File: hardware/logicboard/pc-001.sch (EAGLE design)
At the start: 15 parts, among them J4 DNP, J5 DNP

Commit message: OSHW logo.
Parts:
- added LOGO1: OSHW-LOGOL, SparkFun-Aesthetics:OSHW-LOGOL
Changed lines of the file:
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@@
 <part name="MMA8452Q" library="SparkFun-Connectors" library_urn="urn:adsk.eagle:library:513" deviceset="CONN_06" device="NO_SILK_FEMALE_PTH" package3d_urn="urn:adsk.eagle:package:38130/1"/>
 <part name="FRAME2" library="frames" library_urn="urn:adsk.eagle:library:229" deviceset="A4L-LOC" device=""/>
+<part name="LOGO1" library="SparkFun-Aesthetics" deviceset="OSHW-LOGO" device="L"/>
 </parts>
 <sheets>
@@
 <instance part="MMA8452Q" gate="G$1" x="187.96" y="86.36" rot="R180"/>
 <instance part="FRAME2" gate="G$1" x="0" y="0"/>
+<instance part="LOGO1" gate="G$1" x="200.66" y="15.24"/>
 </instances>
 <busses>

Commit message: Pineapple logo v2.
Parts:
- added U$1: PINEAPPLELOGO2, pineapplelogo2:PINEAPPLELOGO2
- LOGO1: value OSHW-LOGOL -> OSHW-LOGOS-COPPER; device SparkFun-Aesthetics:OSHW-LOGOL -> SparkFun-Aesthetics:OSHW-LOGOS-COPPER
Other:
- note added: "PineappleCake 1.0.0 for MKR1000"
- note removed: "PineappleCake 1000 1.0.0"
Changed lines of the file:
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@@
 <layer number="59" name="tCarbon" color="7" fill="1" visible="no" active="no"/>
 <layer number="60" name="bCarbon" color="7" fill="1" visible="no" active="no"/>
+<layer number="88" name="SimResults" color="9" fill="1" visible="yes" active="yes"/>
+<layer number="89" name="SimProbes" color="9" fill="1" visible="yes" active="yes"/>
 <layer number="90" name="Modules" color="5" fill="1" visible="yes" active="yes"/>
 <layer number="91" name="Nets" color="2" fill="1" visible="yes" active="yes"/>
@@
 <part name="MMA8452Q" library="SparkFun-Connectors" library_urn="urn:adsk.eagle:library:513" deviceset="CONN_06" device="NO_SILK_FEMALE_PTH" package3d_urn="urn:adsk.eagle:package:38130/1"/>
 <part name="FRAME2" library="frames" library_urn="urn:adsk.eagle:library:229" deviceset="A4L-LOC" device=""/>
-<part name="LOGO1" library="SparkFun-Aesthetics" deviceset="OSHW-LOGO" device="L"/>
+<part name="LOGO1" library="SparkFun-Aesthetics" deviceset="OSHW-LOGO" device="S-COPPER"/>
+<part name="U$1" library="pineapplelogo2" deviceset="PINEAPPLELOGO2" device=""/>
 </parts>
 <sheets>
 <sheet>
 <plain>
-<text x="218.44" y="20.32" size="1.778" layer="94">PineappleCake 1000 1.0.0</text>
+<text x="215.9" y="20.32" size="1.778" layer="94">PineappleCake 1.0.0 for MKR1000</text>
 </plain>
 <instances>
@@
 <instance part="MMA8452Q" gate="G$1" x="187.96" y="86.36" rot="R180"/>
 <instance part="FRAME2" gate="G$1" x="0" y="0"/>
-<instance part="LOGO1" gate="G$1" x="200.66" y="15.24"/>
+<instance part="LOGO1" gate="G$1" x="241.3" y="165.1"/>
+<instance part="U$1" gate="G$1" x="187.96" y="7.62"/>
 </instances>
 <busses>

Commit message: New pineapple logo.
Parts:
- removed U$1: PINEAPPLELOGO2, pineapplelogo2:PINEAPPLELOGO2
- added U$2: PINEAPPLELOGO2SILKMINI, pineapplelogo:PINEAPPLELOGO2SILKMINI
- LOGO1: value OSHW-LOGOS-COPPER -> OSHW-LOGOS; device SparkFun-Aesthetics:OSHW-LOGOS-COPPER -> SparkFun-Aesthetics:OSHW-LOGOS
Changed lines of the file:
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@@
 <part name="MMA8452Q" library="SparkFun-Connectors" library_urn="urn:adsk.eagle:library:513" deviceset="CONN_06" device="NO_SILK_FEMALE_PTH" package3d_urn="urn:adsk.eagle:package:38130/1"/>
 <part name="FRAME2" library="frames" library_urn="urn:adsk.eagle:library:229" deviceset="A4L-LOC" device=""/>
-<part name="LOGO1" library="SparkFun-Aesthetics" deviceset="OSHW-LOGO" device="S-COPPER"/>
-<part name="U$1" library="pineapplelogo2" deviceset="PINEAPPLELOGO2" device=""/>
+<part name="LOGO1" library="SparkFun-Aesthetics" deviceset="OSHW-LOGO" device="S" value="OSHW-LOGOS"/>
+<part name="U$2" library="pineapplelogo" deviceset="PINEAPPLELOGO2SILKMINI" device=""/>
 </parts>
 <sheets>
@@
 <instance part="FRAME2" gate="G$1" x="0" y="0"/>
 <instance part="LOGO1" gate="G$1" x="241.3" y="165.1"/>
-<instance part="U$1" gate="G$1" x="187.96" y="7.62"/>
+<instance part="U$2" gate="G$1" x="187.96" y="7.62"/>
 </instances>
 <busses>

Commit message: Updated silk pattern.
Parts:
- renumbered LED1 to L1, LED2 to L2
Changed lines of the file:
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@@
 <part name="C1" library="resistor" library_urn="urn:adsk.eagle:library:348" deviceset="C-US" device="025-025X050" package3d_urn="urn:adsk.eagle:package:26151/1" value="0.1u"/>
 <part name="ANALOG" library="con-ml" library_urn="urn:adsk.eagle:library:164" deviceset="ML14L" device="" package3d_urn="urn:adsk.eagle:package:8677/1"/>
-<part name="LED1" library="SparkFun-Connectors" library_urn="urn:adsk.eagle:library:513" deviceset="CONN_02" device="-JST-2-PTH-NO_SILK" package3d_urn="urn:adsk.eagle:package:38056/1"/>
-<part name="LED2" library="SparkFun-Connectors" library_urn="urn:adsk.eagle:library:513" deviceset="CONN_02" device="-JST-2-PTH-NO_SILK" package3d_urn="urn:adsk.eagle:package:38056/1"/>
+<part name="L1" library="SparkFun-Connectors" library_urn="urn:adsk.eagle:library:513" deviceset="CONN_02" device="-JST-2-PTH-NO_SILK" package3d_urn="urn:adsk.eagle:package:38056/1"/>
+<part name="L2" library="SparkFun-Connectors" library_urn="urn:adsk.eagle:library:513" deviceset="CONN_02" device="-JST-2-PTH-NO_SILK" package3d_urn="urn:adsk.eagle:package:38056/1"/>
 <part name="I2C" library="SparkFun-Connectors" library_urn="urn:adsk.eagle:library:513" deviceset="CONN_05" device="SMD" package3d_urn="urn:adsk.eagle:package:38026/1" value="3.3V"/>
 <part name="SUPPLY3" library="supply2" library_urn="urn:adsk.eagle:library:372" deviceset="GND" device=""/>
@@
 <instance part="C1" gate="G$1" x="134.62" y="99.06"/>
 <instance part="ANALOG" gate="1" x="93.98" y="127" rot="MR180"/>
-<instance part="LED1" gate="G$1" x="157.48" y="88.9" rot="R180"/>
-<instance part="LED2" gate="G$1" x="157.48" y="73.66" rot="R180"/>
+<instance part="L1" gate="G$1" x="157.48" y="88.9" rot="R180"/>
+<instance part="L2" gate="G$1" x="157.48" y="73.66" rot="R180"/>
 <instance part="I2C" gate="G$1" x="190.5" y="58.42" rot="R180"/>
 <instance part="SUPPLY3" gate="GND" x="177.8" y="48.26"/>
@@
 <wire x1="86.36" y1="78.74" x2="86.36" y2="68.58" width="0.1524" layer="91"/>
 <wire x1="86.36" y1="68.58" x2="144.78" y2="68.58" width="0.1524" layer="91"/>
-<pinref part="LED1" gate="G$1" pin="2"/>
+<pinref part="L1" gate="G$1" pin="2"/>
 <wire x1="144.78" y1="68.58" x2="144.78" y2="86.36" width="0.1524" layer="91"/>
 <wire x1="144.78" y1="86.36" x2="149.86" y2="86.36" width="0.1524" layer="91"/>
@@
 <net name="LED2K" class="0">
 <segment>
-<pinref part="LED2" gate="G$1" pin="2"/>
+<pinref part="L2" gate="G$1" pin="2"/>
 <wire x1="149.86" y1="71.12" x2="147.32" y2="71.12" width="0.1524" layer="91"/>
 <wire x1="147.32" y1="71.12" x2="147.32" y2="66.04" width="0.1524" layer="91"/>
@@
 <pinref part="R1" gate="G$1" pin="1"/>
 <wire x1="139.7" y1="91.44" x2="139.7" y2="88.9" width="0.1524" layer="91"/>
-<pinref part="LED1" gate="G$1" pin="1"/>
+<pinref part="L1" gate="G$1" pin="1"/>
 <wire x1="139.7" y1="88.9" x2="149.86" y2="88.9" width="0.1524" layer="91"/>
 </segment>
@@
 <pinref part="R2" gate="G$1" pin="1"/>
 <wire x1="142.24" y1="76.2" x2="142.24" y2="73.66" width="0.1524" layer="91"/>
-<pinref part="LED2" gate="G$1" pin="1"/>
+<pinref part="L2" gate="G$1" pin="1"/>
 <wire x1="142.24" y1="73.66" x2="149.86" y2="73.66" width="0.1524" layer="91"/>
 </segment>

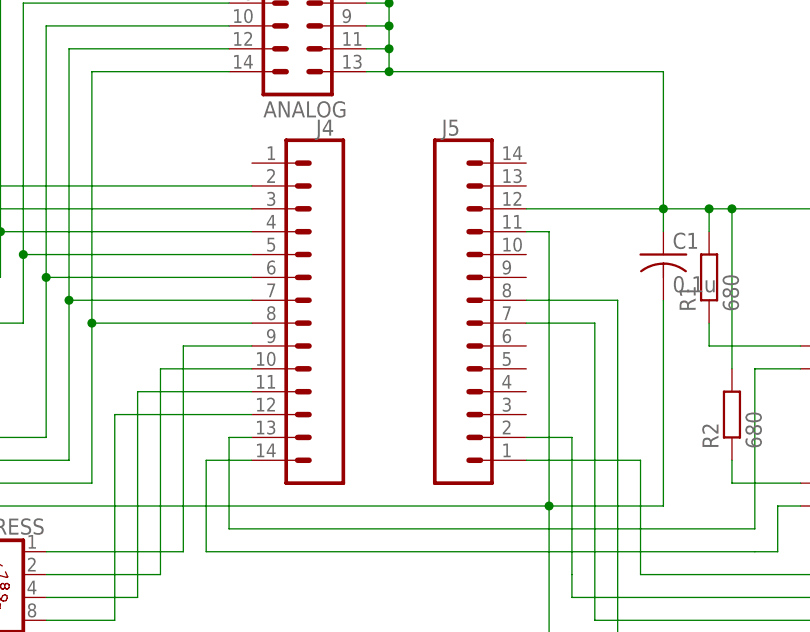
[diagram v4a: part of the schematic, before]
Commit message: Changed signal names.
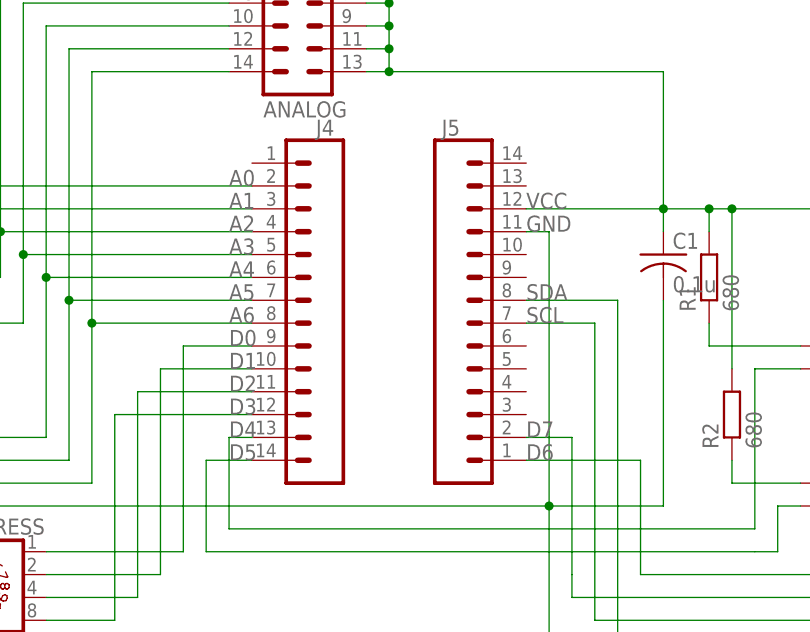
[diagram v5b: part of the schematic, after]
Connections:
- net LED1K renamed D4
- net LED2K renamed D5
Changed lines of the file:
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@@
 <pinref part="ANALOG" gate="1" pin="2"/>
 <wire x1="55.88" y1="134.62" x2="86.36" y2="134.62" width="0.1524" layer="91"/>
+<label x="86.36" y="106.68" size="1.778" layer="95"/>
 </segment>
 </net>
@@
 <pinref part="ANALOG" gate="1" pin="4"/>
 <wire x1="58.42" y1="132.08" x2="86.36" y2="132.08" width="0.1524" layer="91"/>
+<label x="86.36" y="104.14" size="1.778" layer="95"/>
 </segment>
 </net>
@@
 <wire x1="134.62" y1="93.98" x2="134.62" y2="71.12" width="0.1524" layer="91"/>
 <wire x1="134.62" y1="71.12" x2="121.92" y2="71.12" width="0.1524" layer="91"/>
+<label x="119.38" y="101.6" size="1.778" layer="95"/>
 </segment>
 <segment>
@@
 <junction x="177.8" y="91.44"/>
 <label x="177.8" y="91.44" size="1.778" layer="95"/>
+<label x="119.38" y="104.14" size="1.778" layer="95"/>
 </segment>
 </net>
@@
 <pinref part="IPADDRESS" gate="1" pin="1"/>
 <wire x1="81.28" y1="66.04" x2="66.04" y2="66.04" width="0.1524" layer="91"/>
+<label x="86.36" y="88.9" size="1.778" layer="95"/>
 </segment>
 </net>
@@
 <pinref part="IPADDRESS" gate="1" pin="2"/>
 <wire x1="78.74" y1="63.5" x2="66.04" y2="63.5" width="0.1524" layer="91"/>
+<label x="86.36" y="86.36" size="1.778" layer="95"/>
 </segment>
 </net>
@@
 <pinref part="IPADDRESS" gate="1" pin="4"/>
 <wire x1="76.2" y1="60.96" x2="66.04" y2="60.96" width="0.1524" layer="91"/>
+<label x="86.36" y="83.82" size="1.778" layer="95"/>
 </segment>
 </net>
@@
 <pinref part="IPADDRESS" gate="1" pin="8"/>
 <wire x1="73.66" y1="58.42" x2="66.04" y2="58.42" width="0.1524" layer="91"/>
+<label x="86.36" y="81.28" size="1.778" layer="95"/>
 </segment>
 </net>
@@
 <pinref part="ANALOG" gate="1" pin="6"/>
 <wire x1="60.96" y1="129.54" x2="86.36" y2="129.54" width="0.1524" layer="91"/>
+<label x="86.36" y="101.6" size="1.778" layer="95"/>
 </segment>
 </net>
@@
 <pinref part="ANALOG" gate="1" pin="8"/>
 <wire x1="63.5" y1="127" x2="86.36" y2="127" width="0.1524" layer="91"/>
+<label x="86.36" y="99.06" size="1.778" layer="95"/>
 </segment>
 </net>
@@
 <pinref part="ANALOG" gate="1" pin="10"/>
 <wire x1="66.04" y1="124.46" x2="86.36" y2="124.46" width="0.1524" layer="91"/>
+<label x="86.36" y="96.52" size="1.778" layer="95"/>
 </segment>
 </net>
@@
 <pinref part="ANALOG" gate="1" pin="12"/>
 <wire x1="68.58" y1="121.92" x2="86.36" y2="121.92" width="0.1524" layer="91"/>
+<label x="86.36" y="93.98" size="1.778" layer="95"/>
 </segment>
 </net>
@@
 <pinref part="ANALOG" gate="1" pin="14"/>
 <wire x1="71.12" y1="119.38" x2="86.36" y2="119.38" width="0.1524" layer="91"/>
-</segment>
-</net>
-<net name="LED1K" class="0">
+<label x="86.36" y="91.44" size="1.778" layer="95"/>
+</segment>
+</net>
+<net name="D4" class="0">
 <segment>
 <pinref part="J4" gate="G$1" pin="13"/>
@@
 <wire x1="144.78" y1="68.58" x2="144.78" y2="86.36" width="0.1524" layer="91"/>
 <wire x1="144.78" y1="86.36" x2="149.86" y2="86.36" width="0.1524" layer="91"/>
-</segment>
-</net>
-<net name="LED2K" class="0">
+<label x="86.36" y="78.74" size="1.778" layer="95"/>
+</segment>
+</net>
+<net name="D5" class="0">
 <segment>
 <pinref part="L2" gate="G$1" pin="2"/>
@@
 <pinref part="J4" gate="G$1" pin="14"/>
 <wire x1="83.82" y1="76.2" x2="88.9" y2="76.2" width="0.1524" layer="91"/>
+<label x="86.36" y="76.2" size="1.778" layer="95"/>
 </segment>
 </net>
@@
 <junction x="170.18" y="60.96"/>
 <label x="177.8" y="83.82" size="1.778" layer="95"/>
+<label x="119.38" y="78.74" size="1.778" layer="95"/>
 </segment>
 </net>
@@
 <junction x="175.26" y="86.36"/>
 <label x="177.8" y="86.36" size="1.778" layer="95"/>
+<label x="119.38" y="91.44" size="1.778" layer="95"/>
 </segment>
 </net>
@@
 <junction x="172.72" y="88.9"/>
 <label x="177.8" y="88.9" size="1.778" layer="95"/>
+<label x="119.38" y="93.98" size="1.778" layer="95"/>
 </segment>
 </net>
@@
 <wire x1="167.64" y1="81.28" x2="182.88" y2="81.28" width="0.1524" layer="91"/>
 <label x="177.8" y="81.28" size="1.778" layer="95"/>
-</segment>
-</net>
+<label x="119.38" y="76.2" size="1.778" layer="95"/>
+</segment>
+</net>

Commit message: Version number 1.0.0 -> 2.0.0.
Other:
- note added: "PineappleCake 2.0.0 for MKR1000"
- note removed: "PineappleCake 1.0.0 for MKR1000"
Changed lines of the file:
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@@
 <sheet>
 <plain>
-<text x="215.9" y="20.32" size="1.778" layer="94">PineappleCake 1.0.0 for MKR1000</text>
+<text x="215.9" y="20.32" size="1.778" layer="94">PineappleCake 2.0.0 for MKR1000</text>
 </plain>
 <instances>

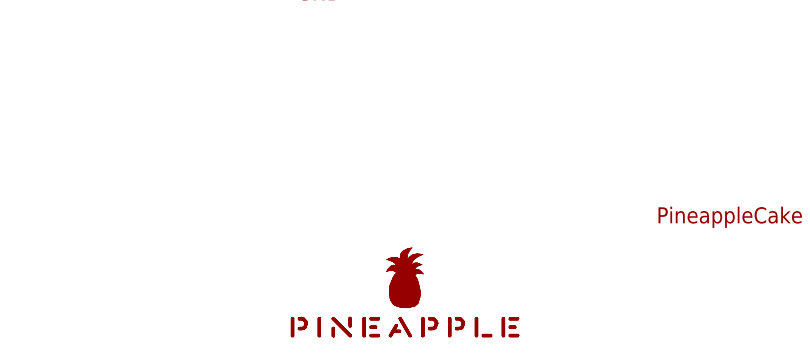
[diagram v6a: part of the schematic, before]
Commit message: Changed Pineapple Logo from Vector-based to Bitmap-based.
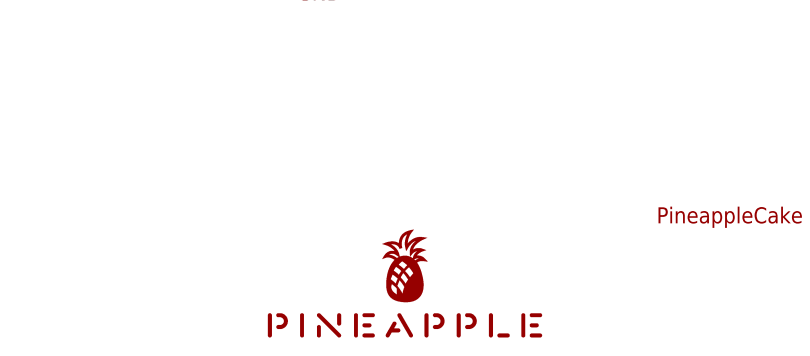
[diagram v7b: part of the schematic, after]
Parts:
- removed U$2: PINEAPPLELOGO2SILKMINI, pineapplelogo:PINEAPPLELOGO2SILKMINI
- added U$1: PINEAPPLE450, pineapple:PINEAPPLE450
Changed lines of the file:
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@@
 <part name="FRAME2" library="frames" library_urn="urn:adsk.eagle:library:229" deviceset="A4L-LOC" device=""/>
 <part name="LOGO1" library="SparkFun-Aesthetics" deviceset="OSHW-LOGO" device="S" value="OSHW-LOGOS"/>
-<part name="U$2" library="pineapplelogo" deviceset="PINEAPPLELOGO2SILKMINI" device=""/>
+<part name="U$1" library="pineapple" deviceset="PINEAPPLE450" device=""/>
 </parts>
 <sheets>
@@
 <instance part="FRAME2" gate="G$1" x="0" y="0"/>
 <instance part="LOGO1" gate="G$1" x="241.3" y="165.1"/>
-<instance part="U$2" gate="G$1" x="187.96" y="7.62"/>
+<instance part="U$1" gate="G$1" x="187.96" y="7.62"/>
 </instances>
 <busses>

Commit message: OSHW logo (silk -> copper).
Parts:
- LOGO1: value OSHW-LOGOS -> OSHW-LOGOS-COPPER; device SparkFun-Aesthetics:OSHW-LOGOS -> SparkFun-Aesthetics:OSHW-LOGOS-COPPER
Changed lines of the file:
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@@
 <part name="MMA8452Q" library="SparkFun-Connectors" library_urn="urn:adsk.eagle:library:513" deviceset="CONN_06" device="NO_SILK_FEMALE_PTH" package3d_urn="urn:adsk.eagle:package:38130/1"/>
 <part name="FRAME2" library="frames" library_urn="urn:adsk.eagle:library:229" deviceset="A4L-LOC" device=""/>
-<part name="LOGO1" library="SparkFun-Aesthetics" deviceset="OSHW-LOGO" device="S" value="OSHW-LOGOS"/>
+<part name="LOGO1" library="SparkFun-Aesthetics" deviceset="OSHW-LOGO" device="S-COPPER" value="OSHW-LOGOS-COPPER"/>
 <part name="U$1" library="pineapple" deviceset="PINEAPPLE450" device=""/>
 </parts>
